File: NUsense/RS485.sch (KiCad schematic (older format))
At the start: 8 parts, among them J18? MOLEX22-03-5045, U21? MAX3443ECSA+

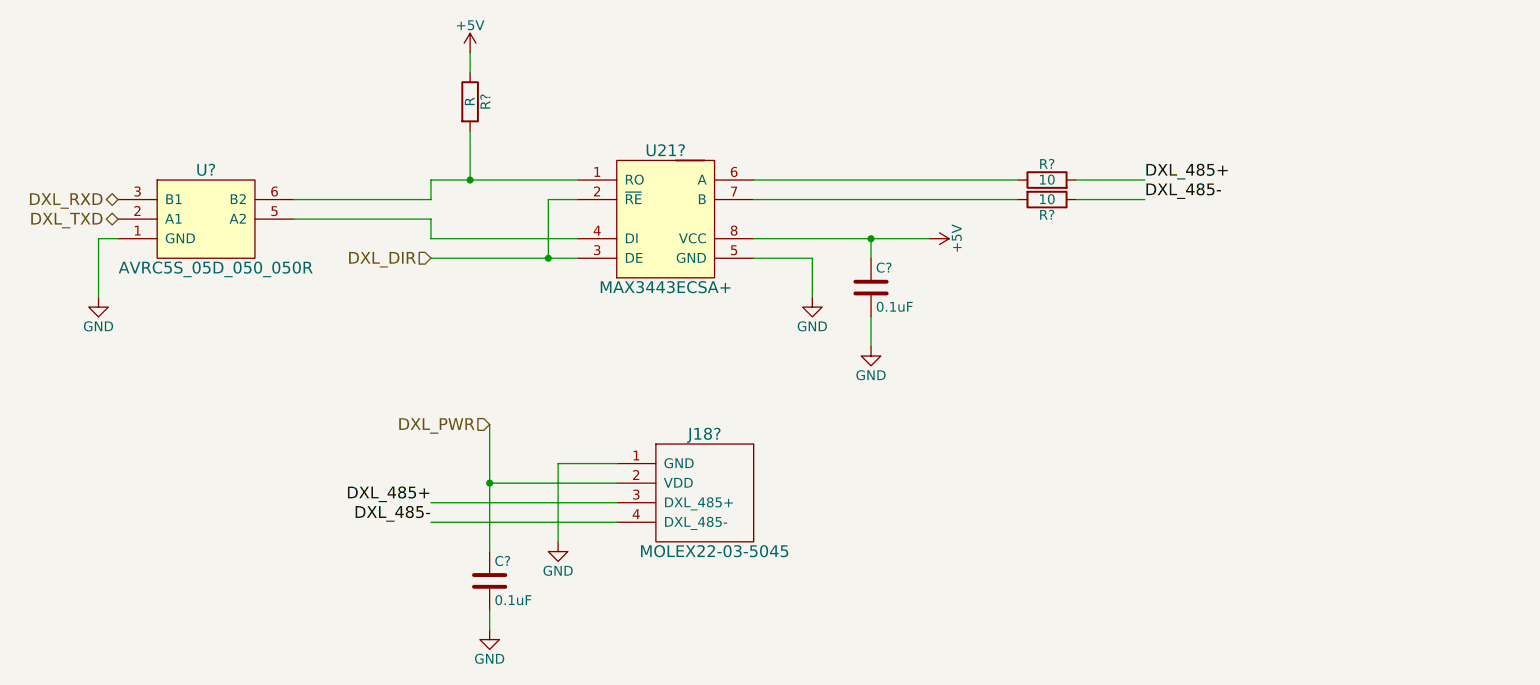
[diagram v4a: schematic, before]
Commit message: Adds annotations and footprints to all components
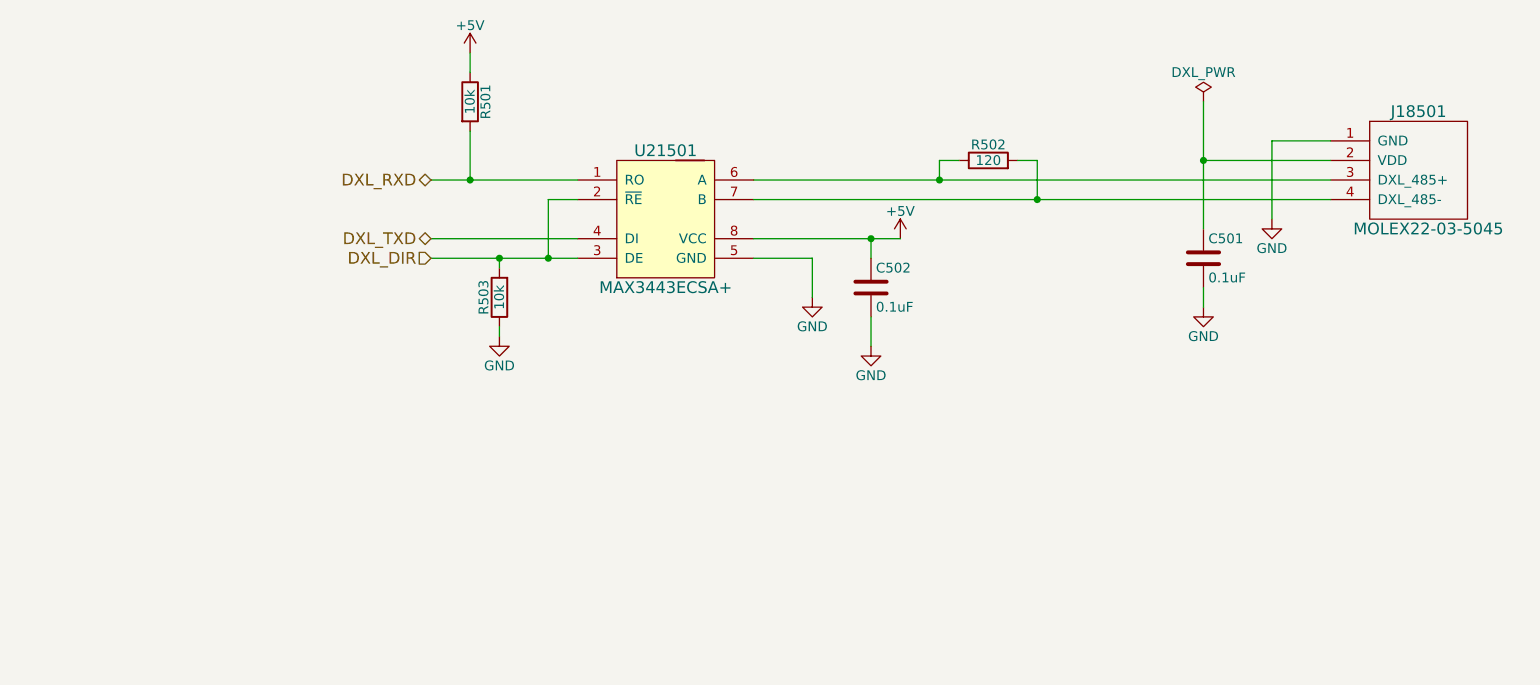
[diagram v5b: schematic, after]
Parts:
- removed R?: 10, symbol R
- removed U?: AVRC5S_05D_050_050R, symbol AVRC5S_05D_050_050R
- added R503: 10k, Resistors_SMD:R_0805_HandSoldering, symbol R
- C501, C502: renamed from C?; footprint (none) -> Capacitors_SMD:C_0805_HandSoldering
- R501: renamed from R?; value R -> 10k; footprint (none) -> Resistors_SMD:R_0805_HandSoldering
- R502: renamed from R?; value 10 -> 120; footprint (none) -> Resistors_SMD:R_0805_HandSoldering
- U21501: renamed from U21?; footprint (none) -> Footprints:MAX3443E
- gave numbers to parts that had none: 1
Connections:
- net DXL_485- is gone; now on an unnamed net: J18501.4 (DXL_485-)
- net DXL_DIR: now also R503.2
- net DXL_RXD: now also R501.2, U21501.1 (RO)
- net DXL_TXD: now also U21501.4 (DI)
- net GND: now also R503.1
- net at R502.1, U21501.6 (A): now also J18501.3 (DXL_485+)
- net at U21501.7 (B): now also R502.2
- removed net DXL_485+: J18501.3 (DXL_485+), R502.2
- net DXL_PWR: no longer names the net of C501.1, J18501.2 (VDD)
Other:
- moved on the sheet: C501, J18501, R502
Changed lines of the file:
@@
 $Descr A3 16535 11693
 encoding utf-8
-Sheet 5 9
+Sheet 5 12
 Title ""
 Date ""
@@
 $EndDescr
 $Comp
-L MAX3443ECSA+ U21?
+L MAX3443ECSA+ U21501
 U 1 1 5A698B5D
 P 4500 3700
-F 0 "U21?" H 4750 4350 60  0000 C CNN
+F 0 "U21501" H 4750 4350 60  0000 C CNN
 F 1 "MAX3443ECSA+" H 4750 3650 60  0000 C CNN
-F 2 "" H 4500 3700 60  0001 C CNN
+F 2 "Footprints:MAX3443E" H 4500 3700 60  0001 C CNN
 F 3 "" H 4500 3700 60  0001 C CNN
 	1    4500 3700
@@
 $EndComp
 $Comp
-L R R?
+L R R501
 U 1 1 5A698BD3
 P 3750 2800
-F 0 "R?" V 3830 2800 50  0000 C CNN
-F 1 "R" V 3750 2800 50  0000 C CNN
-F 2 "" V 3680 2800 50  0001 C CNN
+F 0 "R501" V 3830 2800 50  0000 C CNN
+F 1 "10k" V 3750 2800 50  0000 C CNN
+F 2 "Resistors_SMD:R_0805_HandSoldering" V 3680 2800 50  0001 C CNN
 F 3 "" H 3750 2800 50  0001 C CNN
 	1    3750 2800
@@
 $EndComp
 $Comp
-L GND #PWR?
+L GND #PWR505
 U 1 1 5A698C04
 P 5500 3800
-F 0 "#PWR?" H 5500 3550 50  0001 C CNN
+F 0 "#PWR505" H 5500 3550 50  0001 C CNN
 F 1 "GND" H 5500 3650 50  0000 C CNN
 F 2 "" H 5500 3800 50  0001 C CNN
@@
 $EndComp
 $Comp
-L GND #PWR?
+L GND #PWR506
 U 1 1 5A698C36
 P 5800 4050
-F 0 "#PWR?" H 5800 3800 50  0001 C CNN
+F 0 "#PWR506" H 5800 3800 50  0001 C CNN
 F 1 "GND" H 5800 3900 50  0000 C CNN
 F 2 "" H 5800 4050 50  0001 C CNN
@@
 $EndComp
 $Comp
-L C C?
+L C C502
 U 1 1 5A698C47
 P 5800 3750
-F 0 "C?" H 5825 3850 50  0000 L CNN
+F 0 "C502" H 5825 3850 50  0000 L CNN
 F 1 "0.1uF" H 5825 3650 50  0000 L CNN
-F 2 "" H 5838 3600 50  0001 C CNN
+F 2 "Capacitors_SMD:C_0805_HandSoldering" H 5838 3600 50  0001 C CNN
 F 3 "" H 5800 3750 50  0001 C CNN
 	1    5800 3750
@@
 $EndComp
 $Comp
-L R R?
-U 1 1 5A698C8E
-P 6700 3300
-F 0 "R?" V 6780 3300 50  0000 C CNN
-F 1 "10" V 6700 3300 50  0000 C CNN
-F 2 "" V 6630 3300 50  0001 C CNN
-F 3 "" H 6700 3300 50  0001 C CNN
-	1    6700 3300
-	0    1    1    0
-$EndComp
-$Comp
-L R R?
+L R R502
 U 1 1 5A698D2E
-P 6700 3200
-F 0 "R?" V 6780 3200 50  0000 C CNN
-F 1 "10" V 6700 3200 50  0000 C CNN
-F 2 "" V 6630 3200 50  0001 C CNN
-F 3 "" H 6700 3200 50  0001 C CNN
-	1    6700 3200
+P 6400 3100
+F 0 "R502" V 6480 3100 50  0000 C CNN
+F 1 "120" V 6400 3100 50  0000 C CNN
+F 2 "Resistors_SMD:R_0805_HandSoldering" V 6330 3100 50  0001 C CNN
+F 3 "" H 6400 3100 50  0001 C CNN
+	1    6400 3100
 	0    -1   -1   0
 $EndComp
 $Comp
-L GND #PWR?
+L GND #PWR504
 U 1 1 5A6992FB
-P 4200 5050
-F 0 "#PWR?" H 4200 4800 50  0001 C CNN
-F 1 "GND" H 4200 4900 50  0000 C CNN
-F 2 "" H 4200 5050 50  0001 C CNN
-F 3 "" H 4200 5050 50  0001 C CNN
-	1    4200 5050
-	1    0    0    -1
-$EndComp
-$Comp
-L C C?
+P 7850 3400
+F 0 "#PWR504" H 7850 3150 50  0001 C CNN
+F 1 "GND" H 7850 3250 50  0000 C CNN
+F 2 "" H 7850 3400 50  0001 C CNN
+F 3 "" H 7850 3400 50  0001 C CNN
+	1    7850 3400
+	1    0    0    -1
+$EndComp
+$Comp
+L C C501
 U 1 1 5A699329
-P 3850 5250
-F 0 "C?" H 3875 5350 50  0000 L CNN
-F 1 "0.1uF" H 3875 5150 50  0000 L CNN
-F 2 "" H 3888 5100 50  0001 C CNN
-F 3 "" H 3850 5250 50  0001 C CNN
-	1    3850 5250
-	1    0    0    -1
-$EndComp
-$Comp
-L GND #PWR?
+P 7500 3600
+F 0 "C501" H 7525 3700 50  0000 L CNN
+F 1 "0.1uF" H 7525 3500 50  0000 L CNN
+F 2 "Capacitors_SMD:C_0805_HandSoldering" H 7538 3450 50  0001 C CNN
+F 3 "" H 7500 3600 50  0001 C CNN
+	1    7500 3600
+	1    0    0    -1
+$EndComp
+$Comp
+L GND #PWR503
 U 1 1 5A69938B
-P 3850 5500
-F 0 "#PWR?" H 3850 5250 50  0001 C CNN
-F 1 "GND" H 3850 5350 50  0000 C CNN
-F 2 "" H 3850 5500 50  0001 C CNN
-F 3 "" H 3850 5500 50  0001 C CNN
-	1    3850 5500
-	1    0    0    -1
-$EndComp
-Wire Wire Line
-	3550 3600 4150 3600
-Wire Wire Line
-	4150 3600 4300 3600
+P 7500 3850
+F 0 "#PWR503" H 7500 3600 50  0001 C CNN
+F 1 "GND" H 7500 3700 50  0000 C CNN
+F 2 "" H 7500 3850 50  0001 C CNN
+F 3 "" H 7500 3850 50  0001 C CNN
+	1    7500 3850
+	1    0    0    -1
+$EndComp
+Wire Wire Line
+	3550 3600 4300 3600
 Wire Wire Line
 	4300 3500 3550 3500
 Wire Wire Line
-	3550 3200 3750 3200
-Wire Wire Line
-	3750 3200 4300 3200
+	3550 3200 4300 3200
 Wire Wire Line
 	4300 3300 4150 3300
@@
 	3750 2550 3750 2650
 Wire Wire Line
-	6550 3200 5200 3200
-Wire Wire Line
-	5200 3300 6550 3300
-Wire Wire Line
-	5200 3500 5800 3500
-Wire Wire Line
-	5800 3500 6100 3500
+	5200 3200 8150 3200
+Wire Wire Line
+	5200 3300 8150 3300
 Wire Wire Line
 	5800 3600 5800 3500
@@
 	5500 3600 5200 3600
 Wire Wire Line
-	7200 3300 6850 3300
-Wire Wire Line
-	6850 3200 7200 3200
-Wire Wire Line
-	4500 4850 3550 4850
-Wire Wire Line
-	4500 4950 3550 4950
-Wire Wire Line
-	3850 5500 3850 5400
-Wire Wire Line
-	3850 4450 3850 4750
-Wire Wire Line
-	3850 4750 3850 5100
-Wire Wire Line
-	3850 4750 4500 4750
-Connection ~ 3850 4750
-Wire Wire Line
-	4200 5050 4200 4650
-Wire Wire Line
-	4200 4650 4500 4650
-$Comp
-L MOLEX22-03-5045 J18?
+	7500 3850 7500 3750
+Wire Wire Line
+	7500 2800 7500 3450
+Wire Wire Line
+	7500 3100 8150 3100
+Connection ~ 7500 3100
+Wire Wire Line
+	7850 3400 7850 3000
+Wire Wire Line
+	7850 3000 8150 3000
+$Comp
+L MOLEX22-03-5045 J18501
 U 1 1 5A6A7E14
-P 4700 4800
-F 0 "J18?" H 4950 5100 60  0000 C CNN
-F 1 "MOLEX22-03-5045" H 5000 4500 60  0000 C CNN
-F 2 "" H 4700 4800 60  0001 C CNN
-F 3 "" H 4700 4800 60  0001 C CNN
-	1    4700 4800
-	1    0    0    -1
-$EndComp
-$Comp
-L +5V #PWR?
+P 8350 3150
+F 0 "J18501" H 8600 3450 60  0000 C CNN
+F 1 "MOLEX22-03-5045" H 8650 2850 60  0000 C CNN
+F 2 "" H 8350 3150 60  0001 C CNN
+F 3 "" H 8350 3150 60  0001 C CNN
+	1    8350 3150
+	1    0    0    -1
+$EndComp
+$Comp
+L +5V #PWR502
 U 1 1 5A6FDCF8
 P 3750 2550
-F 0 "#PWR?" H 3750 2400 50  0001 C CNN
+F 0 "#PWR502" H 3750 2400 50  0001 C CNN
 F 1 "+5V" H 3750 2690 50  0000 C CNN
 F 2 "" H 3750 2550 50  0001 C CNN
@@
 	1    0    0    -1
 $EndComp
-Text HLabel 1950 3300 0    60   BiDi ~ 0
+Text HLabel 3550 3200 0    60   BiDi ~ 0
 DXL_RXD
-Text HLabel 1950 3400 0    60   BiDi ~ 0
+Text HLabel 3550 3500 0    60   BiDi ~ 0
 DXL_TXD
 Text HLabel 3550 3600 0    60   Input ~ 0
 DXL_DIR
 $Comp
-L +5V #PWR?
+L +5V #PWR507
 U 1 1 5A6FED8C
-P 6100 3500
-F 0 "#PWR?" H 6100 3350 50  0001 C CNN
-F 1 "+5V" H 6100 3640 50  0000 C CNN
-F 2 "" H 6100 3500 50  0001 C CNN
-F 3 "" H 6100 3500 50  0001 C CNN
-	1    6100 3500
-	0    1    1    0
-$EndComp
-Text Label 7200 3200 0    60   ~ 0
-DXL_485+
-Text Label 7200 3300 0    60   ~ 0
-DXL_485-
-Text Label 3550 4850 2    60   ~ 0
-DXL_485+
-Text Label 3550 4950 2    60   ~ 0
-DXL_485-
-Text HLabel 3850 4450 0    60   Input ~ 0
-DXL_PWR
-$Comp
-L AVRC5S_05D_050_050R U?
-U 1 1 5A72D5C4
-P 2150 3600
-F 0 "U?" H 2400 4050 60  0000 C CNN
-F 1 "AVRC5S_05D_050_050R" H 2450 3550 60  0000 C CNN
-F 2 "" H 2150 3600 60  0001 C CNN
-F 3 "" H 2150 3600 60  0001 C CNN
-	1    2150 3600
-	1    0    0    -1
-$EndComp
-Wire Wire Line
-	2850 3300 3550 3300
-Wire Wire Line
-	3550 3300 3550 3200
-Wire Wire Line
-	3550 3500 3550 3400
-Wire Wire Line
-	3550 3400 2850 3400
-Wire Wire Line
-	1950 3500 1850 3500
-Wire Wire Line
-	1850 3500 1850 3800
+P 5950 3500
+F 0 "#PWR507" H 5950 3350 50  0001 C CNN
+F 1 "+5V" H 5950 3640 50  0000 C CNN
+F 2 "" H 5950 3500 50  0001 C CNN
+F 3 "" H 5950 3500 50  0001 C CNN
+	1    5950 3500
+	1    0    0    -1
+$EndComp
+$Comp
+L DXL_PWR #FLG?
+U 1 1 5A75309D
+P 7500 2800
+F 0 "#FLG?" H 7500 2875 50  0001 C CNN
+F 1 "DXL_PWR" H 7500 2950 50  0000 C CNN
+F 2 "" H 7500 2800 50  0001 C CNN
+F 3 "" H 7500 2800 50  0001 C CNN
+	1    7500 2800
+	1    0    0    -1
+$EndComp
+Wire Wire Line
+	5950 3500 5200 3500
+Wire Wire Line
+	6250 3100 6150 3100
+Wire Wire Line
+	6150 3100 6150 3200
+Connection ~ 6150 3200
+Wire Wire Line
+	6550 3100 6650 3100
+Wire Wire Line
+	6650 3100 6650 3300
+Connection ~ 6650 3300
+$Comp
+L R R503
+U 1 1 5A75344C
+P 3900 3800
+F 0 "R503" V 3980 3800 50  0000 C CNN
+F 1 "10k" V 3900 3800 50  0000 C CNN
+F 2 "Resistors_SMD:R_0805_HandSoldering" V 3830 3800 50  0001 C CNN
+F 3 "" H 3900 3800 50  0001 C CNN
+	1    3900 3800
+	-1   0    0    1
+$EndComp
 $Comp
 L GND #PWR?
-U 1 1 5A72D76F
-P 1850 3800
-F 0 "#PWR?" H 1850 3550 50  0001 C CNN
-F 1 "GND" H 1850 3650 50  0000 C CNN
-F 2 "" H 1850 3800 50  0001 C CNN
-F 3 "" H 1850 3800 50  0001 C CNN
-	1    1850 3800
-	1    0    0    -1
-$EndComp
+U 1 1 5A7534E4
+P 3900 4000
+F 0 "#PWR?" H 3900 3750 50  0001 C CNN
+F 1 "GND" H 3900 3850 50  0000 C CNN
+F 2 "" H 3900 4000 50  0001 C CNN
+F 3 "" H 3900 4000 50  0001 C CNN
+	1    3900 4000
+	1    0    0    -1
+$EndComp
+Wire Wire Line
+	3900 3650 3900 3600
+Connection ~ 3900 3600
+Wire Wire Line
+	3900 3950 3900 4000
 $EndSCHEMATC

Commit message: More Changes
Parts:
- renumbered C502 to C1101, C501 to C1102, J18501 to J1101, R501 to R1101, R503 to R1102, R502 to R1103, U21501 to U1101
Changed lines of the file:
@@
 $Descr A3 16535 11693
 encoding utf-8
-Sheet 5 12
+Sheet 11 12
 Title ""
 Date ""
@@
 $EndDescr
 $Comp
-L MAX3443ECSA+ U21501
+L MAX3443ECSA+ U1101
 U 1 1 5A698B5D
 P 4500 3700
-F 0 "U21501" H 4750 4350 60  0000 C CNN
+AR Path="/5A751354/5A698B5D" Ref="U1101"  Part="1"
+AR Path="/5A698B54/5A698B5D" Ref="U501"  Part="1"
+AR Path="/5A74FCE6/5A698B5D" Ref="U801"  Part="1"
+AR Path="/5A750BFE/5A698B5D" Ref="U901"  Part="1"
+AR Path="/5A750C08/5A698B5D" Ref="U1001"  Part="1"
+F 0 "U1101" H 4750 4350 60  0000 C CNN
 F 1 "MAX3443ECSA+" H 4750 3650 60  0000 C CNN
 F 2 "Footprints:MAX3443E" H 4500 3700 60  0001 C CNN
@@
 $EndComp
 $Comp
-L R R501
+L R R1101
 U 1 1 5A698BD3
 P 3750 2800
-F 0 "R501" V 3830 2800 50  0000 C CNN
+AR Path="/5A751354/5A698BD3" Ref="R1101"  Part="1"
+AR Path="/5A698B54/5A698BD3" Ref="R501"  Part="1"
+AR Path="/5A74FCE6/5A698BD3" Ref="R801"  Part="1"
+AR Path="/5A750BFE/5A698BD3" Ref="R901"  Part="1"
+AR Path="/5A750C08/5A698BD3" Ref="R1001"  Part="1"
+F 0 "R1101" V 3830 2800 50  0000 C CNN
 F 1 "10k" V 3750 2800 50  0000 C CNN
 F 2 "Resistors_SMD:R_0805_HandSoldering" V 3680 2800 50  0001 C CNN
@@
 $EndComp
 $Comp
-L GND #PWR505
+L GND #PWR0101
 U 1 1 5A698C04
 P 5500 3800
-F 0 "#PWR505" H 5500 3550 50  0001 C CNN
+AR Path="/5A751354/5A698C04" Ref="#PWR0101"  Part="1"
+AR Path="/5A698B54/5A698C04" Ref="#PWR039"  Part="1"
+AR Path="/5A74FCE6/5A698C04" Ref="#PWR077"  Part="1"
+AR Path="/5A750BFE/5A698C04" Ref="#PWR085"  Part="1"
+AR Path="/5A750C08/5A698C04" Ref="#PWR093"  Part="1"
+F 0 "#PWR0101" H 5500 3550 50  0001 C CNN
 F 1 "GND" H 5500 3650 50  0000 C CNN
 F 2 "" H 5500 3800 50  0001 C CNN
@@
 $EndComp
 $Comp
-L GND #PWR506
+L GND #PWR0102
 U 1 1 5A698C36
 P 5800 4050
-F 0 "#PWR506" H 5800 3800 50  0001 C CNN
+AR Path="/5A751354/5A698C36" Ref="#PWR0102"  Part="1"
+AR Path="/5A698B54/5A698C36" Ref="#PWR040"  Part="1"
+AR Path="/5A74FCE6/5A698C36" Ref="#PWR078"  Part="1"
+AR Path="/5A750BFE/5A698C36" Ref="#PWR086"  Part="1"
+AR Path="/5A750C08/5A698C36" Ref="#PWR094"  Part="1"
+F 0 "#PWR0102" H 5800 3800 50  0001 C CNN
 F 1 "GND" H 5800 3900 50  0000 C CNN
 F 2 "" H 5800 4050 50  0001 C CNN
@@
 $EndComp
 $Comp
-L C C502
+L C C1101
 U 1 1 5A698C47
 P 5800 3750
-F 0 "C502" H 5825 3850 50  0000 L CNN
+AR Path="/5A751354/5A698C47" Ref="C1101"  Part="1"
+AR Path="/5A698B54/5A698C47" Ref="C501"  Part="1"
+AR Path="/5A74FCE6/5A698C47" Ref="C801"  Part="1"
+AR Path="/5A750BFE/5A698C47" Ref="C901"  Part="1"
+AR Path="/5A750C08/5A698C47" Ref="C1001"  Part="1"
+F 0 "C1101" H 5825 3850 50  0000 L CNN
 F 1 "0.1uF" H 5825 3650 50  0000 L CNN
 F 2 "Capacitors_SMD:C_0805_HandSoldering" H 5838 3600 50  0001 C CNN
@@
 $EndComp
 $Comp
-L R R502
+L R R1103
 U 1 1 5A698D2E
 P 6400 3100
-F 0 "R502" V 6480 3100 50  0000 C CNN
+AR Path="/5A751354/5A698D2E" Ref="R1103"  Part="1"
+AR Path="/5A698B54/5A698D2E" Ref="R503"  Part="1"
+AR Path="/5A74FCE6/5A698D2E" Ref="R803"  Part="1"
+AR Path="/5A750BFE/5A698D2E" Ref="R903"  Part="1"
+AR Path="/5A750C08/5A698D2E" Ref="R1003"  Part="1"
+F 0 "R1103" V 6480 3100 50  0000 C CNN
 F 1 "120" V 6400 3100 50  0000 C CNN
 F 2 "Resistors_SMD:R_0805_HandSoldering" V 6330 3100 50  0001 C CNN
@@
 $EndComp
 $Comp
-L GND #PWR504
+L GND #PWR0103
 U 1 1 5A6992FB
 P 7850 3400
-F 0 "#PWR504" H 7850 3150 50  0001 C CNN
+AR Path="/5A751354/5A6992FB" Ref="#PWR0103"  Part="1"
+AR Path="/5A698B54/5A6992FB" Ref="#PWR041"  Part="1"
+AR Path="/5A74FCE6/5A6992FB" Ref="#PWR079"  Part="1"
+AR Path="/5A750BFE/5A6992FB" Ref="#PWR087"  Part="1"
+AR Path="/5A750C08/5A6992FB" Ref="#PWR095"  Part="1"
+F 0 "#PWR0103" H 7850 3150 50  0001 C CNN
 F 1 "GND" H 7850 3250 50  0000 C CNN
 F 2 "" H 7850 3400 50  0001 C CNN
@@
 $EndComp
 $Comp
-L C C501
-U 1 1 5A699329
-P 7500 3600
-F 0 "C501" H 7525 3700 50  0000 L CNN
-F 1 "0.1uF" H 7525 3500 50  0000 L CNN
-F 2 "Capacitors_SMD:C_0805_HandSoldering" H 7538 3450 50  0001 C CNN
-F 3 "" H 7500 3600 50  0001 C CNN
-	1    7500 3600
-	1    0    0    -1
-$EndComp
-$Comp
-L GND #PWR503
+L GND #PWR0104
 U 1 1 5A69938B
 P 7500 3850
-F 0 "#PWR503" H 7500 3600 50  0001 C CNN
+AR Path="/5A751354/5A69938B" Ref="#PWR0104"  Part="1"
+AR Path="/5A698B54/5A69938B" Ref="#PWR042"  Part="1"
+AR Path="/5A74FCE6/5A69938B" Ref="#PWR080"  Part="1"
+AR Path="/5A750BFE/5A69938B" Ref="#PWR088"  Part="1"
+AR Path="/5A750C08/5A69938B" Ref="#PWR096"  Part="1"
+F 0 "#PWR0104" H 7500 3600 50  0001 C CNN
 F 1 "GND" H 7500 3700 50  0000 C CNN
 F 2 "" H 7500 3850 50  0001 C CNN
@@
 	7850 3000 8150 3000
 $Comp
-L MOLEX22-03-5045 J18501
+L MOLEX22-03-5045 J1101
 U 1 1 5A6A7E14
 P 8350 3150
-F 0 "J18501" H 8600 3450 60  0000 C CNN
+AR Path="/5A751354/5A6A7E14" Ref="J1101"  Part="1"
+AR Path="/5A698B54/5A6A7E14" Ref="J501"  Part="1"
+AR Path="/5A74FCE6/5A6A7E14" Ref="J801"  Part="1"
+AR Path="/5A750BFE/5A6A7E14" Ref="J901"  Part="1"
+AR Path="/5A750C08/5A6A7E14" Ref="J1001"  Part="1"
+F 0 "J1101" H 8600 3450 60  0000 C CNN
 F 1 "MOLEX22-03-5045" H 8650 2850 60  0000 C CNN
 F 2 "" H 8350 3150 60  0001 C CNN
@@
 $EndComp
 $Comp
-L +5V #PWR502
+L +5V #PWR0105
 U 1 1 5A6FDCF8
 P 3750 2550
-F 0 "#PWR502" H 3750 2400 50  0001 C CNN
+AR Path="/5A751354/5A6FDCF8" Ref="#PWR0105"  Part="1"
+AR Path="/5A698B54/5A6FDCF8" Ref="#PWR043"  Part="1"
+AR Path="/5A74FCE6/5A6FDCF8" Ref="#PWR081"  Part="1"
+AR Path="/5A750BFE/5A6FDCF8" Ref="#PWR089"  Part="1"
+AR Path="/5A750C08/5A6FDCF8" Ref="#PWR097"  Part="1"
+F 0 "#PWR0105" H 3750 2400 50  0001 C CNN
 F 1 "+5V" H 3750 2690 50  0000 C CNN
 F 2 "" H 3750 2550 50  0001 C CNN
@@
 DXL_DIR
 $Comp
-L +5V #PWR507
+L +5V #PWR0106
 U 1 1 5A6FED8C
 P 5950 3500
-F 0 "#PWR507" H 5950 3350 50  0001 C CNN
+AR Path="/5A751354/5A6FED8C" Ref="#PWR0106"  Part="1"
+AR Path="/5A698B54/5A6FED8C" Ref="#PWR044"  Part="1"
+AR Path="/5A74FCE6/5A6FED8C" Ref="#PWR082"  Part="1"
+AR Path="/5A750BFE/5A6FED8C" Ref="#PWR090"  Part="1"
+AR Path="/5A750C08/5A6FED8C" Ref="#PWR098"  Part="1"
+F 0 "#PWR0106" H 5950 3350 50  0001 C CNN
 F 1 "+5V" H 5950 3640 50  0000 C CNN
 F 2 "" H 5950 3500 50  0001 C CNN
@@
 $EndComp
 $Comp
-L DXL_PWR #FLG?
+L DXL_PWR #FLG0107
 U 1 1 5A75309D
 P 7500 2800
-F 0 "#FLG?" H 7500 2875 50  0001 C CNN
+AR Path="/5A751354/5A75309D" Ref="#FLG0107"  Part="1"
+AR Path="/5A698B54/5A75309D" Ref="#FLG045"  Part="1"
+AR Path="/5A74FCE6/5A75309D" Ref="#FLG083"  Part="1"
+AR Path="/5A750BFE/5A75309D" Ref="#FLG091"  Part="1"
+AR Path="/5A750C08/5A75309D" Ref="#FLG099"  Part="1"
+F 0 "#FLG0107" H 7500 2875 50  0001 C CNN
 F 1 "DXL_PWR" H 7500 2950 50  0000 C CNN
 F 2 "" H 7500 2800 50  0001 C CNN
@@
 Connection ~ 6650 3300
 $Comp
-L R R503
+L R R1102
 U 1 1 5A75344C
 P 3900 3800
-F 0 "R503" V 3980 3800 50  0000 C CNN
+AR Path="/5A751354/5A75344C" Ref="R1102"  Part="1"
+AR Path="/5A698B54/5A75344C" Ref="R502"  Part="1"
+AR Path="/5A74FCE6/5A75344C" Ref="R802"  Part="1"
+AR Path="/5A750BFE/5A75344C" Ref="R902"  Part="1"
+AR Path="/5A750C08/5A75344C" Ref="R1002"  Part="1"
+F 0 "R1102" V 3980 3800 50  0000 C CNN
 F 1 "10k" V 3900 3800 50  0000 C CNN
 F 2 "Resistors_SMD:R_0805_HandSoldering" V 3830 3800 50  0001 C CNN
@@
 $EndComp
 $Comp
-L GND #PWR?
+L GND #PWR0108
 U 1 1 5A7534E4
 P 3900 4000
-F 0 "#PWR?" H 3900 3750 50  0001 C CNN
+AR Path="/5A751354/5A7534E4" Ref="#PWR0108"  Part="1"
+AR Path="/5A698B54/5A7534E4" Ref="#PWR046"  Part="1"
+AR Path="/5A74FCE6/5A7534E4" Ref="#PWR084"  Part="1"
+AR Path="/5A750BFE/5A7534E4" Ref="#PWR092"  Part="1"
+AR Path="/5A750C08/5A7534E4" Ref="#PWR0100"  Part="1"
+F 0 "#PWR0108" H 3900 3750 50  0001 C CNN
 F 1 "GND" H 3900 3850 50  0000 C CNN
 F 2 "" H 3900 4000 50  0001 C CNN
@@
 Wire Wire Line
 	3900 3950 3900 4000
+$Comp
+L C C1102
+U 1 1 5A699329
+P 7500 3600
+AR Path="/5A751354/5A699329" Ref="C1102"  Part="1"
+AR Path="/5A698B54/5A699329" Ref="C502"  Part="1"
+AR Path="/5A74FCE6/5A699329" Ref="C802"  Part="1"
+AR Path="/5A750BFE/5A699329" Ref="C902"  Part="1"
+AR Path="/5A750C08/5A699329" Ref="C1002"  Part="1"
+F 0 "C1102" H 7525 3700 50  0000 L CNN
+F 1 "0.1uF" H 7525 3500 50  0000 L CNN
+F 2 "Capacitors_SMD:C_0805_HandSoldering" H 7538 3450 50  0001 C CNN
+F 3 "" H 7500 3600 50  0001 C CNN
+	1    7500 3600
+	1    0    0    -1
+$EndComp
 $EndSCHEMATC
